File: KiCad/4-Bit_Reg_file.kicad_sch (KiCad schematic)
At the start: 29 parts, among them J1 CLK/RegWrite, U1 74HC173, U10 74HC00, U2 74HC173, U3 74HC173, U4 74HC173, U5 74LS153, U6 74LS153, U7 74LS153, U8 74LS153, U9 74HC238

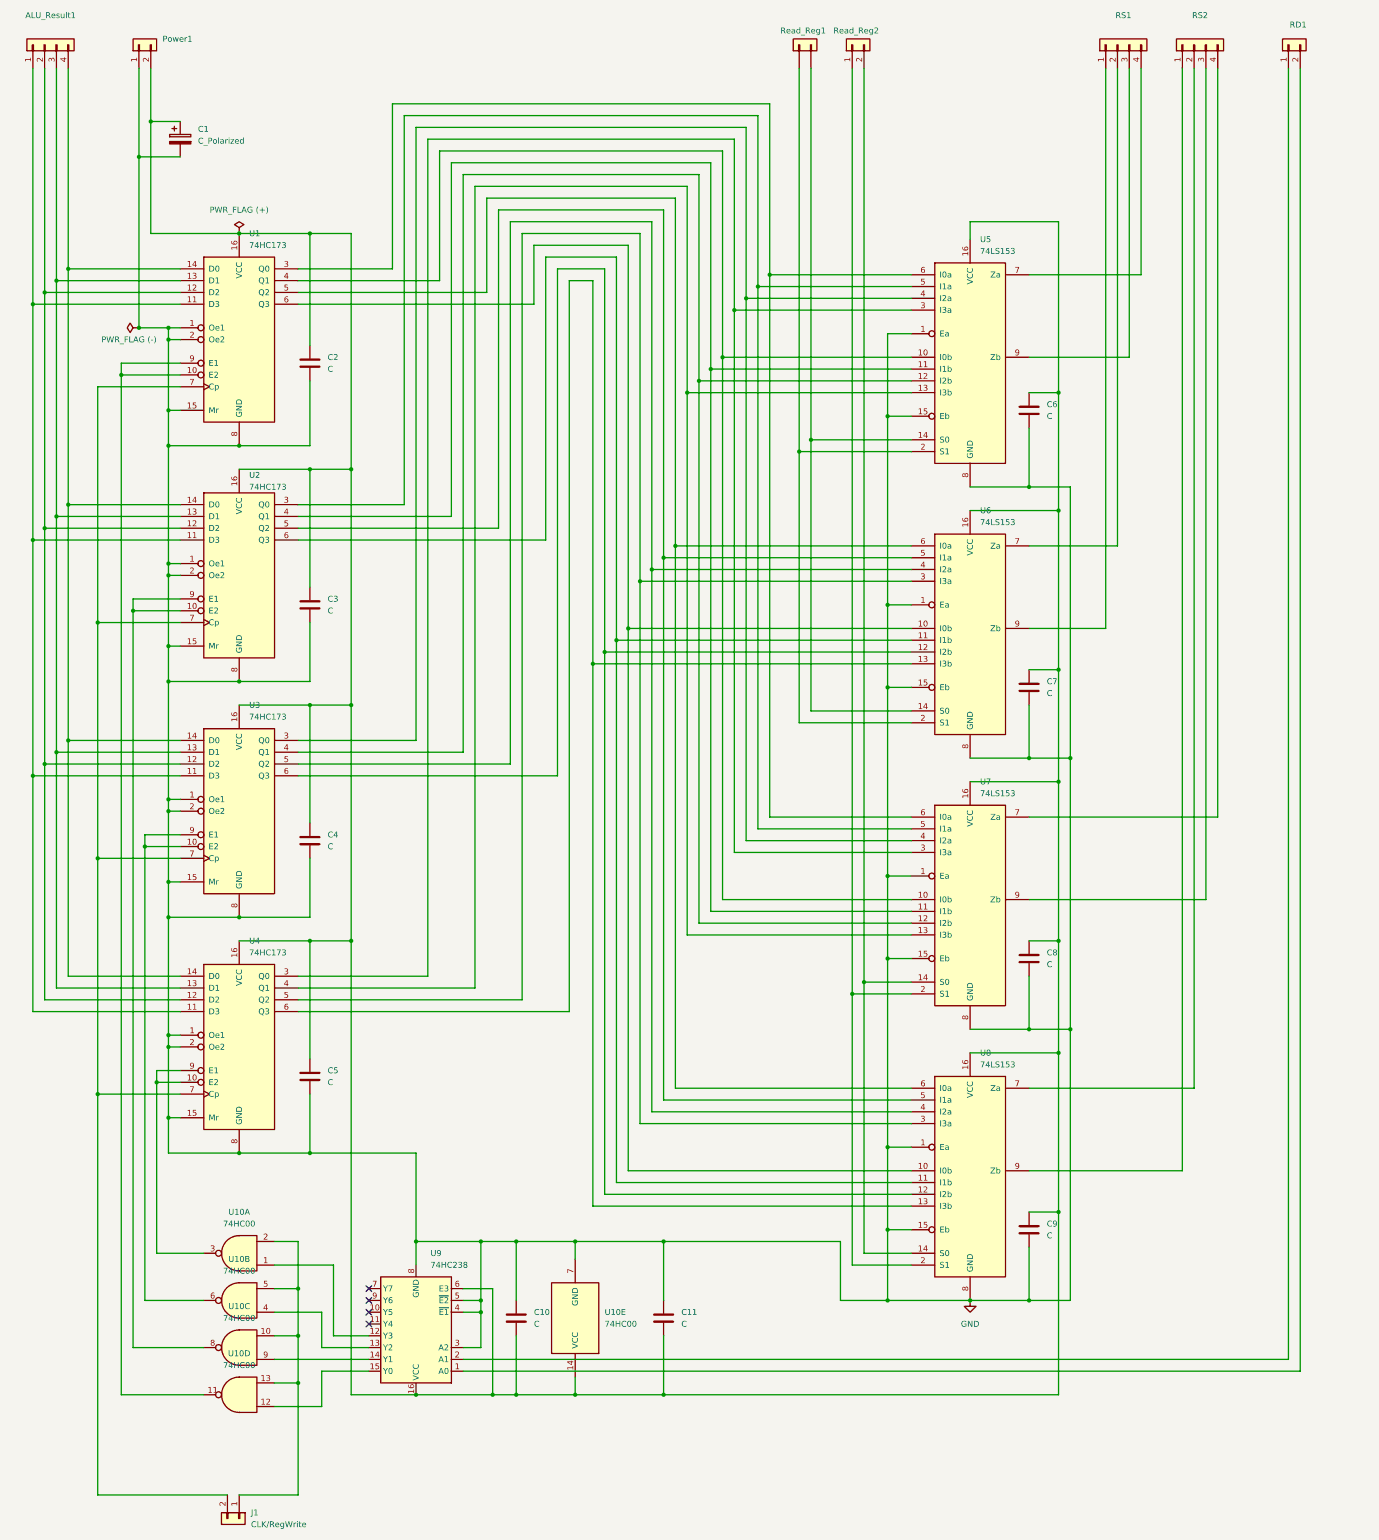
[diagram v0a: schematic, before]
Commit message: Title block added to schematic
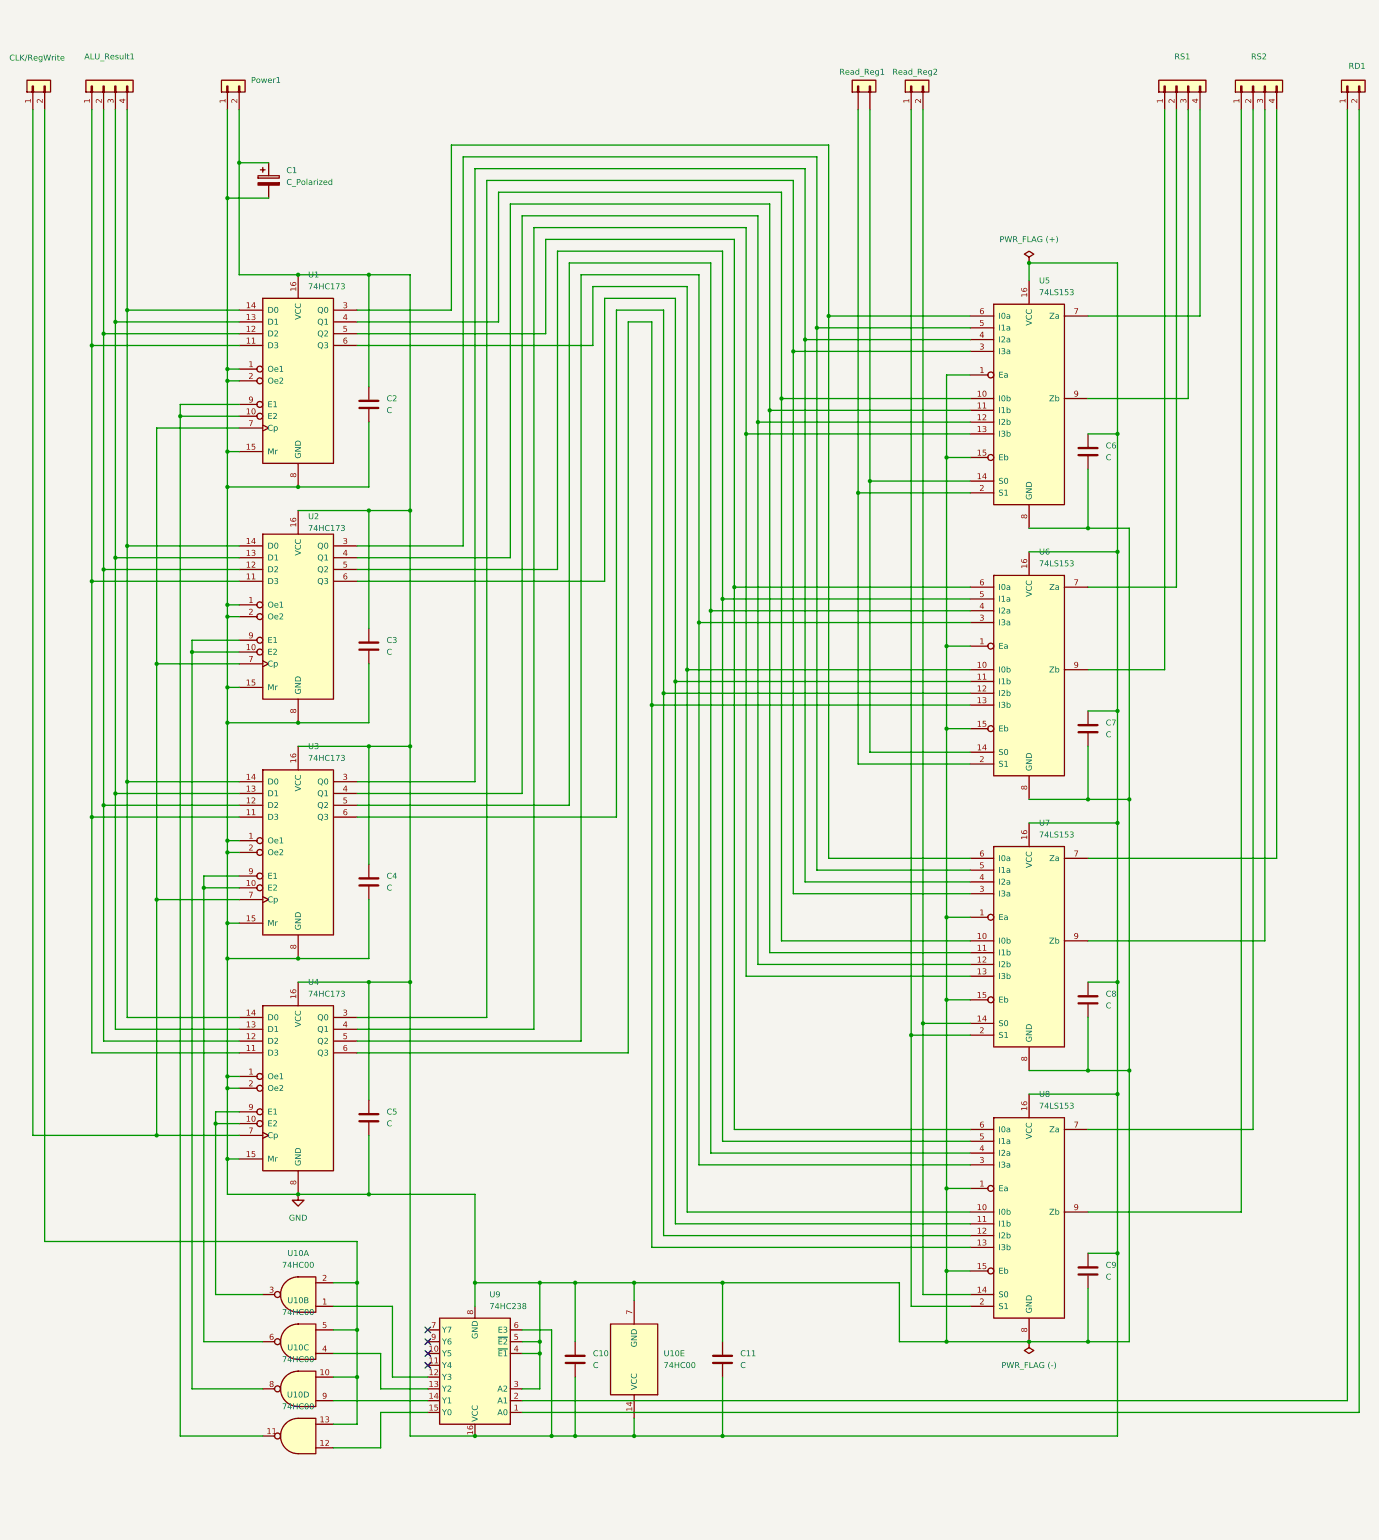
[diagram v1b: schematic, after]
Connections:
- net at U1.7 (Cp), U2.7 (Cp), U3.7 (Cp)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: now also J1.1 (Pin_1); no longer J1.2 (Pin_2)
- net at U10.10, U10.13, U10.2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: now also J1.2 (Pin_2); no longer J1.1 (Pin_1)
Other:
- company: (none) -> Made by: Neowizen 
- title: (none) -> Full 4-Bit Register File RB1534B
- moved on the sheet: ALU_Result1, C1, C10, C11, C2, C3, C4, C5, C6, C7, C8, C9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
